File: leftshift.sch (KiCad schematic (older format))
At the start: 0 parts

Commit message: Progress
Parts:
- added DLS1, DLS2: 1N4148WS, symbol D
- added LS1: MX-2.25U, symbol MX-2.25U
- added LS2: MX-2U, symbol MX-2U
- added MX? (x3): MX-1U, symbol MX-1U
- added MX?: MX-1.25U, symbol MX-1.25U
- added RLS1, RLS2: 2.2k, symbol R
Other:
- note added: "Left Shift Cluster\n"
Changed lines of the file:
@@
 $Descr A4 11693 8268
 encoding utf-8
-Sheet 1 4
+Sheet 4 5
 Title ""
 Date ""
@@
 Comment4 ""
 $EndDescr
+Text Notes 7325 7500 0    60   ~ 0
+Left Shift Cluster\n
+$Comp
+L MX-2.25U LS1
+U 1 1 591A4F37
+P 3750 3000
+F 0 "LS1" H 3750 3125 60  0000 C CNN
+F 1 "MX-2.25U" H 3750 3050 20  0000 C CNN
+F 2 "" H 3725 2975 60  0001 C CNN
+F 3 "" H 3725 2975 60  0001 C CNN
+	1    3750 3000
+	1    0    0    -1
+$EndComp
+$Comp
+L MX-2U LS2
+U 1 1 591A5035
+P 3750 3575
+F 0 "LS2" H 3750 3700 60  0000 C CNN
+F 1 "MX-2U" H 3750 3625 20  0000 C CNN
+F 2 "" H 3725 3550 60  0001 C CNN
+F 3 "" H 3725 3550 60  0001 C CNN
+	1    3750 3575
+	1    0    0    -1
+$EndComp
+$Comp
+L MX-1U MX?
+U 1 1 591A5109
+P 3750 4150
+F 0 "MX?" H 3750 4275 60  0000 C CNN
+F 1 "MX-1U" H 3750 4200 20  0000 C CNN
+F 2 "" H 3725 4125 60  0001 C CNN
+F 3 "" H 3725 4125 60  0001 C CNN
+	1    3750 4150
+	1    0    0    -1
+$EndComp
+$Comp
+L MX-1U MX?
+U 1 1 591A5134
+P 4200 4150
+F 0 "MX?" H 4200 4275 60  0000 C CNN
+F 1 "MX-1U" H 4200 4200 20  0000 C CNN
+F 2 "" H 4175 4125 60  0001 C CNN
+F 3 "" H 4175 4125 60  0001 C CNN
+	1    4200 4150
+	1    0    0    -1
+$EndComp
+$Comp
+L MX-1U MX?
+U 1 1 591A51E1
+P 4200 4725
+F 0 "MX?" H 4200 4850 60  0000 C CNN
+F 1 "MX-1U" H 4200 4775 20  0000 C CNN
+F 2 "" H 4175 4700 60  0001 C CNN
+F 3 "" H 4175 4700 60  0001 C CNN
+	1    4200 4725
+	1    0    0    -1
+$EndComp
+$Comp
+L MX-1.25U MX?
+U 1 1 591A526C
+P 3750 4725
+F 0 "MX?" H 3750 4850 60  0000 C CNN
+F 1 "MX-1.25U" H 3750 4775 20  0000 C CNN
+F 2 "" H 3725 4700 60  0001 C CNN
+F 3 "" H 3725 4700 60  0001 C CNN
+	1    3750 4725
+	1    0    0    -1
+$EndComp
+$Comp
+L D DLS1
+U 1 1 591A55D2
+P 5550 4400
+F 0 "DLS1" H 5550 4500 50  0000 C CNN
+F 1 "1N4148WS" H 5550 4300 50  0000 C CNN
+F 2 "" H 5550 4400 50  0001 C CNN
+F 3 "" H 5550 4400 50  0001 C CNN
+	1    5550 4400
+	0    -1   -1   0
+$EndComp
+$Comp
+L D DLS2
+U 1 1 591A571F
+P 6025 4400
+F 0 "DLS2" H 6025 4500 50  0000 C CNN
+F 1 "1N4148WS" H 6025 4300 50  0000 C CNN
+F 2 "" H 6025 4400 50  0001 C CNN
+F 3 "" H 6025 4400 50  0001 C CNN
+	1    6025 4400
+	0    -1   -1   0
+$EndComp
+$Comp
+L R RLS1
+U 1 1 591A5D8F
+P 5550 3500
+F 0 "RLS1" V 5630 3500 50  0000 C CNN
+F 1 "2.2k" V 5550 3500 50  0000 C CNN
+F 2 "" V 5480 3500 50  0001 C CNN
+F 3 "" H 5550 3500 50  0001 C CNN
+	1    5550 3500
+	1    0    0    -1
+$EndComp
+$Comp
+L R RLS2
+U 1 1 591A5E9C
+P 6025 3500
+F 0 "RLS2" V 6105 3500 50  0000 C CNN
+F 1 "2.2k" V 6025 3500 50  0000 C CNN
+F 2 "" V 5955 3500 50  0001 C CNN
+F 3 "" H 6025 3500 50  0001 C CNN
+	1    6025 3500
+	1    0    0    -1
+$EndComp
 $EndSCHEMATC

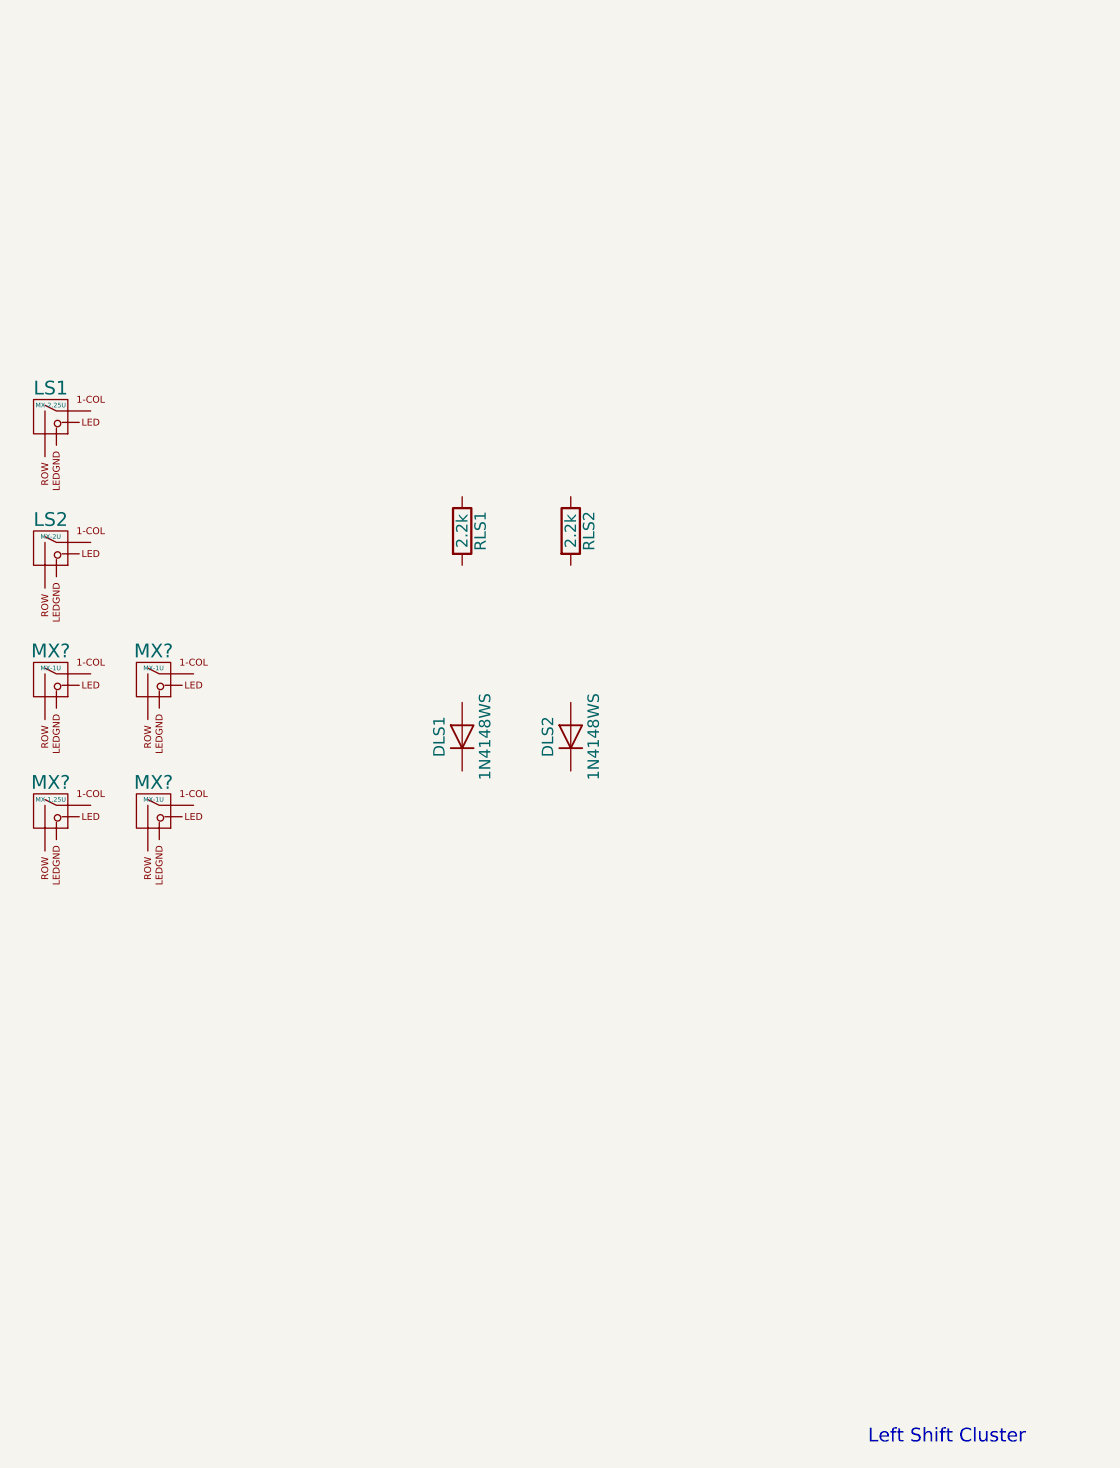
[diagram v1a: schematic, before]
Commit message: Finish Left Shift cluster
Done.
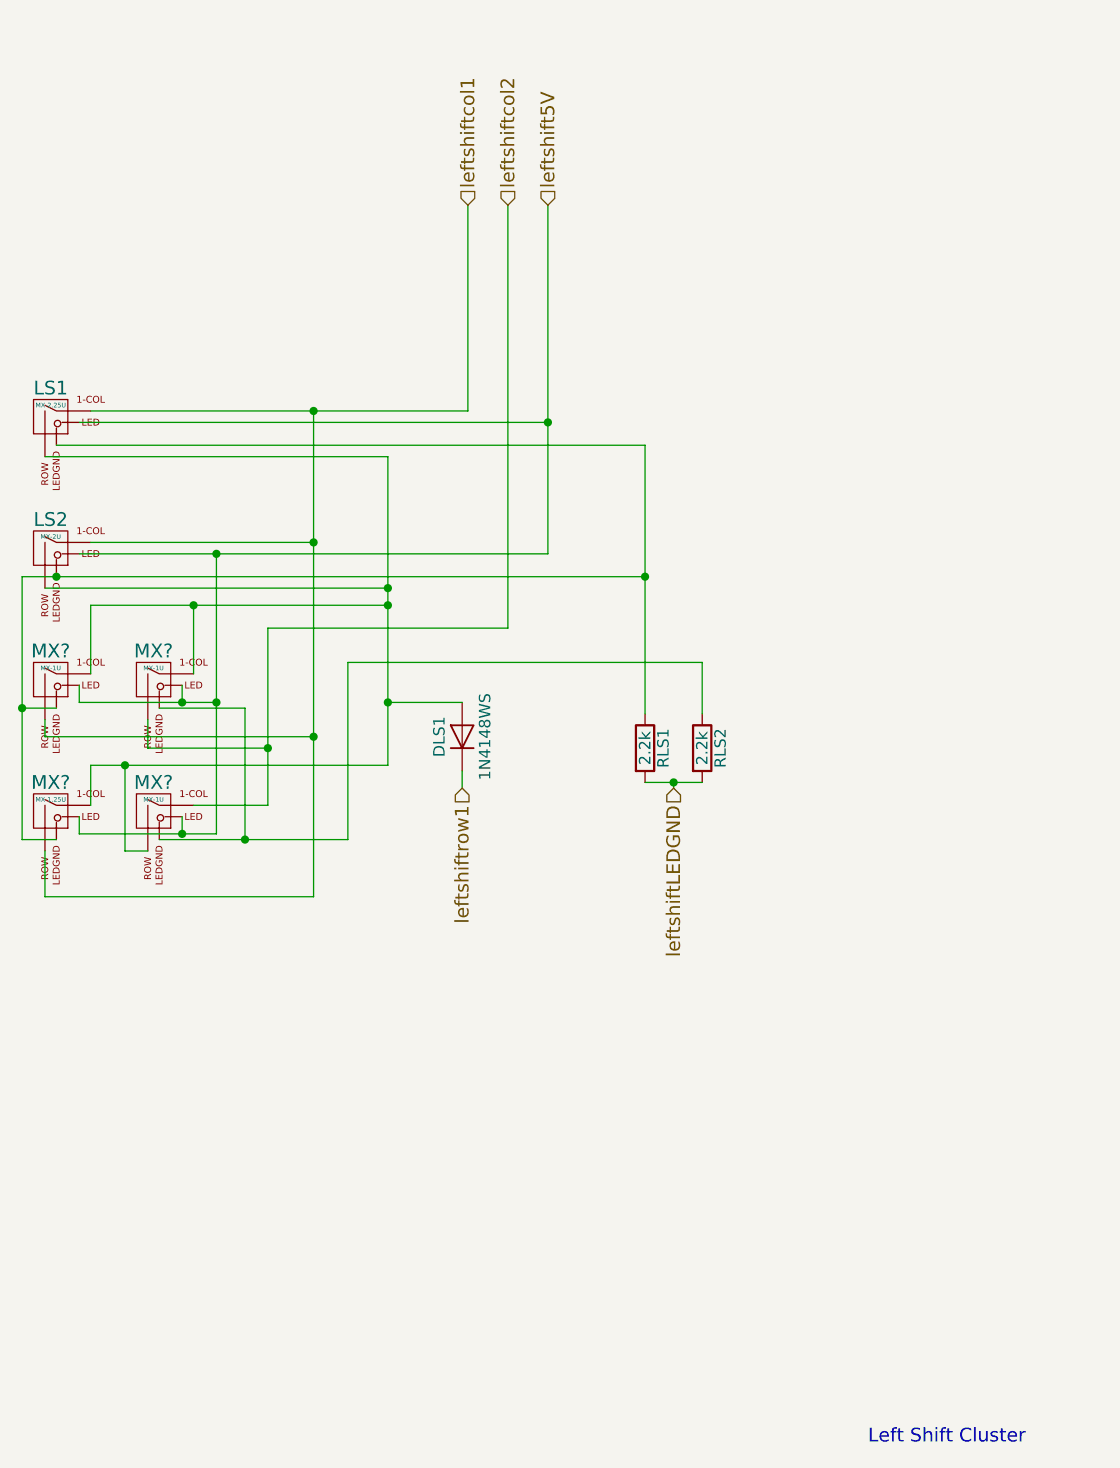
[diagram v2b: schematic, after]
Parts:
- removed DLS2: 1N4148WS, symbol D
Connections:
- net leftshiftcol1: now reaches LS1.1 (COL)
- net leftshiftcol1: now also LS2.1 (COL), MX?.2 (ROW), MX?.2 (ROW)
- net at LS1.2 (ROW): now also DLS1.2 (A), LS2.2 (ROW), MX?.1 (COL), MX?.1 (COL), MX?.1 (COL), MX?.2 (ROW)
- net leftshift5V: now reaches LS1.3 (LED)
- net leftshift5V: now also LS2.3 (LED), MX?.3 (LED), MX?.3 (LED), MX?.3 (LED), MX?.3 (LED)
- net at LS1.4 (LEDGND): now also LS2.4 (LEDGND), MX?.4 (LEDGND), MX?.4 (LEDGND), RLS1.1
- net leftshiftcol2: now reaches MX?.2 (ROW)
- net leftshiftcol2: now also MX?.1 (COL)
- net at MX?.4 (LEDGND): now also MX?.4 (LEDGND), RLS2.1
- net leftshiftrow1: now reaches DLS1.1 (K)
- net leftshiftLEDGND: now reaches RLS1.2
- net leftshiftLEDGND: now also RLS2.2
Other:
- moved on the sheet: RLS1, RLS2
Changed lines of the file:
@@
-$EndComp
-$Comp
-L D DLS2
-U 1 1 591A571F
-P 6025 4400
-F 0 "DLS2" H 6025 4500 50  0000 C CNN
-F 1 "1N4148WS" H 6025 4300 50  0000 C CNN
-F 2 "" H 6025 4400 50  0001 C CNN
-F 3 "" H 6025 4400 50  0001 C CNN
-	1    6025 4400
-	0    -1   -1   0
 $EndComp
 $Comp
 L R RLS1
 U 1 1 591A5D8F
-P 5550 3500
-F 0 "RLS1" V 5630 3500 50  0000 C CNN
-F 1 "2.2k" V 5550 3500 50  0000 C CNN
-F 2 "" V 5480 3500 50  0001 C CNN
-F 3 "" H 5550 3500 50  0001 C CNN
-	1    5550 3500
+P 6350 4450
+F 0 "RLS1" V 6430 4450 50  0000 C CNN
+F 1 "2.2k" V 6350 4450 50  0000 C CNN
+F 2 "" V 6280 4450 50  0001 C CNN
+F 3 "" H 6350 4450 50  0001 C CNN
+	1    6350 4450
 	1    0    0    -1
 $EndComp
@@
 L R RLS2
 U 1 1 591A5E9C
-P 6025 3500
-F 0 "RLS2" V 6105 3500 50  0000 C CNN
-F 1 "2.2k" V 6025 3500 50  0000 C CNN
-F 2 "" V 5955 3500 50  0001 C CNN
-F 3 "" H 6025 3500 50  0001 C CNN
-	1    6025 3500
+P 6600 4450
+F 0 "RLS2" V 6680 4450 50  0000 C CNN
+F 1 "2.2k" V 6600 4450 50  0000 C CNN
+F 2 "" V 6530 4450 50  0001 C CNN
+F 3 "" H 6600 4450 50  0001 C CNN
+	1    6600 4450
 	1    0    0    -1
 $EndComp
+Text HLabel 5575 2075 1    60   Input ~ 0
+leftshiftcol1
+Text HLabel 5750 2075 1    60   Input ~ 0
+leftshiftcol2
+Text HLabel 5550 4625 3    60   Input ~ 0
+leftshiftrow1
+Text HLabel 5925 2075 1    60   Input ~ 0
+leftshift5V
+Text HLabel 6475 4625 3    60   Input ~ 0
+leftshiftLEDGND
+Wire Wire Line
+	5550 4550 5550 4625
+Wire Wire Line
+	3925 2975 5575 2975
+Wire Wire Line
+	5575 2975 5575 2075
+Wire Wire Line
+	3925 3550 4900 3550
+Wire Wire Line
+	4900 2975 4900 5100
+Connection ~ 4900 2975
+Wire Wire Line
+	3725 3175 5225 3175
+Wire Wire Line
+	5225 3175 5225 4525
+Wire Wire Line
+	5225 4250 5550 4250
+Wire Wire Line
+	3725 3750 5225 3750
+Connection ~ 5225 3750
+Wire Wire Line
+	3925 4700 3925 4525
+Wire Wire Line
+	3925 4525 5225 4525
+Connection ~ 5225 4250
+Wire Wire Line
+	4900 5100 3725 5100
+Wire Wire Line
+	3725 5100 3725 4900
+Connection ~ 4900 3550
+Wire Wire Line
+	5750 2075 5750 3925
+Wire Wire Line
+	5750 3925 4700 3925
+Wire Wire Line
+	4700 3925 4700 4700
+Wire Wire Line
+	4700 4700 4375 4700
+Wire Wire Line
+	4175 4900 4075 4900
+Wire Wire Line
+	4075 4900 4075 4525
+Connection ~ 4075 4525
+Wire Wire Line
+	4175 4325 4175 4450
+Wire Wire Line
+	4175 4450 4700 4450
+Connection ~ 4700 4450
+Wire Wire Line
+	4375 4125 4375 3825
+Wire Wire Line
+	3925 3825 5225 3825
+Connection ~ 5225 3825
+Wire Wire Line
+	3925 4125 3925 3825
+Connection ~ 4375 3825
+Wire Wire Line
+	4900 4400 3725 4400
+Wire Wire Line
+	3725 4400 3725 4325
+Connection ~ 4900 4400
+Wire Wire Line
+	6350 4600 6600 4600
+Wire Wire Line
+	6475 4600 6475 4625
+Connection ~ 6475 4600
+Wire Wire Line
+	3875 3025 5925 3025
+Wire Wire Line
+	5925 2075 5925 3600
+Wire Wire Line
+	5925 3600 3875 3600
+Connection ~ 5925 3025
+Wire Wire Line
+	3875 4175 3875 4250
+Wire Wire Line
+	3875 4250 4475 4250
+Wire Wire Line
+	4325 4250 4325 4175
+Wire Wire Line
+	3875 4750 3875 4825
+Wire Wire Line
+	3875 4825 4475 4825
+Wire Wire Line
+	4325 4825 4325 4750
+Wire Wire Line
+	4475 4825 4475 3600
+Connection ~ 4325 4825
+Connection ~ 4325 4250
+Connection ~ 4475 3600
+Connection ~ 4475 4250
+Wire Wire Line
+	3775 3125 6350 3125
+Wire Wire Line
+	6350 3125 6350 4300
+Wire Wire Line
+	3625 3700 6350 3700
+Connection ~ 6350 3700
+Wire Wire Line
+	3775 4275 3625 4275
+Wire Wire Line
+	3625 3700 3625 4850
+Connection ~ 3775 3700
+Wire Wire Line
+	3625 4850 3775 4850
+Connection ~ 3625 4275
+Wire Wire Line
+	4225 4275 4600 4275
+Wire Wire Line
+	4600 4275 4600 4850
+Wire Wire Line
+	4225 4850 5050 4850
+Wire Wire Line
+	5050 4850 5050 4075
+Wire Wire Line
+	5050 4075 6600 4075
+Wire Wire Line
+	6600 4075 6600 4300
+Connection ~ 4600 4850
 $EndSCHEMATC

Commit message: Whoops
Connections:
- net leftshift5V: now also LS1.4 (LEDGND), MX?.4 (LEDGND); no longer LS1.3 (LED), MX?.3 (LED)
- net at LS2.4 (LEDGND), MX?.4 (LEDGND), RLS1.1: now also LS1.3 (LED), MX?.3 (LED); no longer LS1.4 (LEDGND), MX?.4 (LEDGND)
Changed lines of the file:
@@
 Connection ~ 6475 4600
 Wire Wire Line
-	3875 3025 5925 3025
+	4150 3025 5925 3025
 Wire Wire Line
-	5925 2075 5925 3600
+	5925 3600 5925 2075
 Wire Wire Line
-	5925 3600 3875 3600
+	3875 3600 5925 3600
 Connection ~ 5925 3025
 Wire Wire Line
@@
 	4325 4250 4325 4175
 Wire Wire Line
-	3875 4750 3875 4825
-Wire Wire Line
-	3875 4825 4475 4825
+	3825 4825 4475 4825
 Wire Wire Line
 	4325 4825 4325 4750
@@
 Connection ~ 4475 4250
 Wire Wire Line
-	3775 3125 6350 3125
+	4100 3125 6350 3125
 Wire Wire Line
 	6350 3125 6350 4300
@@
 	3775 4275 3625 4275
 Wire Wire Line
-	3625 3700 3625 4850
+	3625 3700 3625 4725
 Connection ~ 3775 3700
-Wire Wire Line
-	3625 4850 3775 4850
 Connection ~ 3625 4275
 Wire Wire Line
@@
 	6600 4075 6600 4300
 Connection ~ 4600 4850
+Wire Wire Line
+	3875 3025 4100 3025
+Wire Wire Line
+	4100 3025 4100 3125
+Wire Wire Line
+	4150 3025 4150 3150
+Wire Wire Line
+	4150 3150 3775 3150
+Wire Wire Line
+	3775 3150 3775 3125
+Wire Wire Line
+	3625 4725 3875 4725
+Wire Wire Line
+	3875 4725 3875 4750
+Wire Wire Line
+	3825 4825 3825 4850
+Wire Wire Line
+	3825 4850 3775 4850
 $EndSCHEMATC

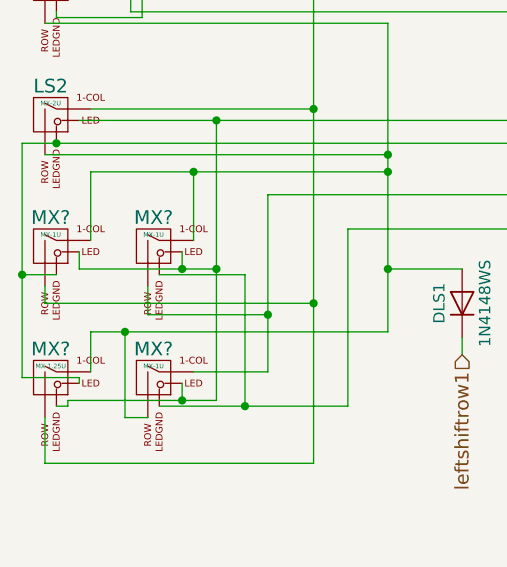
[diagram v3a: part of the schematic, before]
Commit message: Change Left Shift key names
Also synced the source to external backup in case GitHub breaks
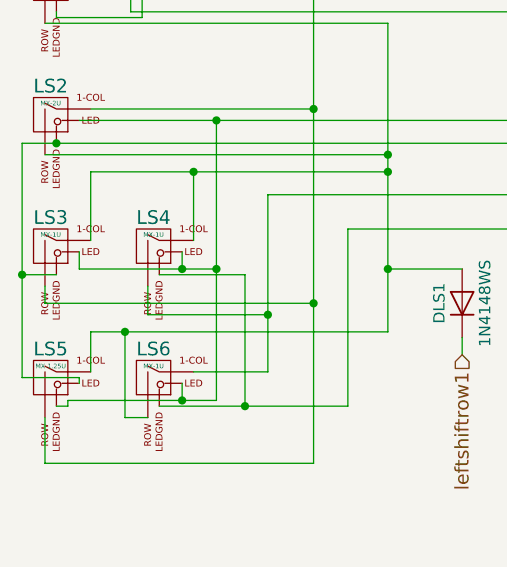
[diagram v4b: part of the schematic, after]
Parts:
- gave numbers to parts that had none: 4
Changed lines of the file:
@@
 $EndComp
 $Comp
-L MX-1U MX?
+L MX-1U LS3
 U 1 1 591A5109
 P 3750 4150
-F 0 "MX?" H 3750 4275 60  0000 C CNN
+F 0 "LS3" H 3750 4275 60  0000 C CNN
 F 1 "MX-1U" H 3750 4200 20  0000 C CNN
 F 2 "" H 3725 4125 60  0001 C CNN
@@
 $EndComp
 $Comp
-L MX-1U MX?
+L MX-1U LS4
 U 1 1 591A5134
 P 4200 4150
-F 0 "MX?" H 4200 4275 60  0000 C CNN
+F 0 "LS4" H 4200 4275 60  0000 C CNN
 F 1 "MX-1U" H 4200 4200 20  0000 C CNN
 F 2 "" H 4175 4125 60  0001 C CNN
@@
 $EndComp
 $Comp
-L MX-1U MX?
+L MX-1U LS6
 U 1 1 591A51E1
 P 4200 4725
-F 0 "MX?" H 4200 4850 60  0000 C CNN
+F 0 "LS6" H 4200 4850 60  0000 C CNN
 F 1 "MX-1U" H 4200 4775 20  0000 C CNN
 F 2 "" H 4175 4700 60  0001 C CNN
@@
 $EndComp
 $Comp
-L MX-1.25U MX?
+L MX-1.25U LS5
 U 1 1 591A526C
 P 3750 4725
-F 0 "MX?" H 3750 4850 60  0000 C CNN
+F 0 "LS5" H 3750 4850 60  0000 C CNN
 F 1 "MX-1.25U" H 3750 4775 20  0000 C CNN
 F 2 "" H 3725 4700 60  0001 C CNN
